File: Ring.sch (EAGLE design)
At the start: 23 parts, among them U1 BQ25125YFPR, U3 NRF52832-CIAA-R

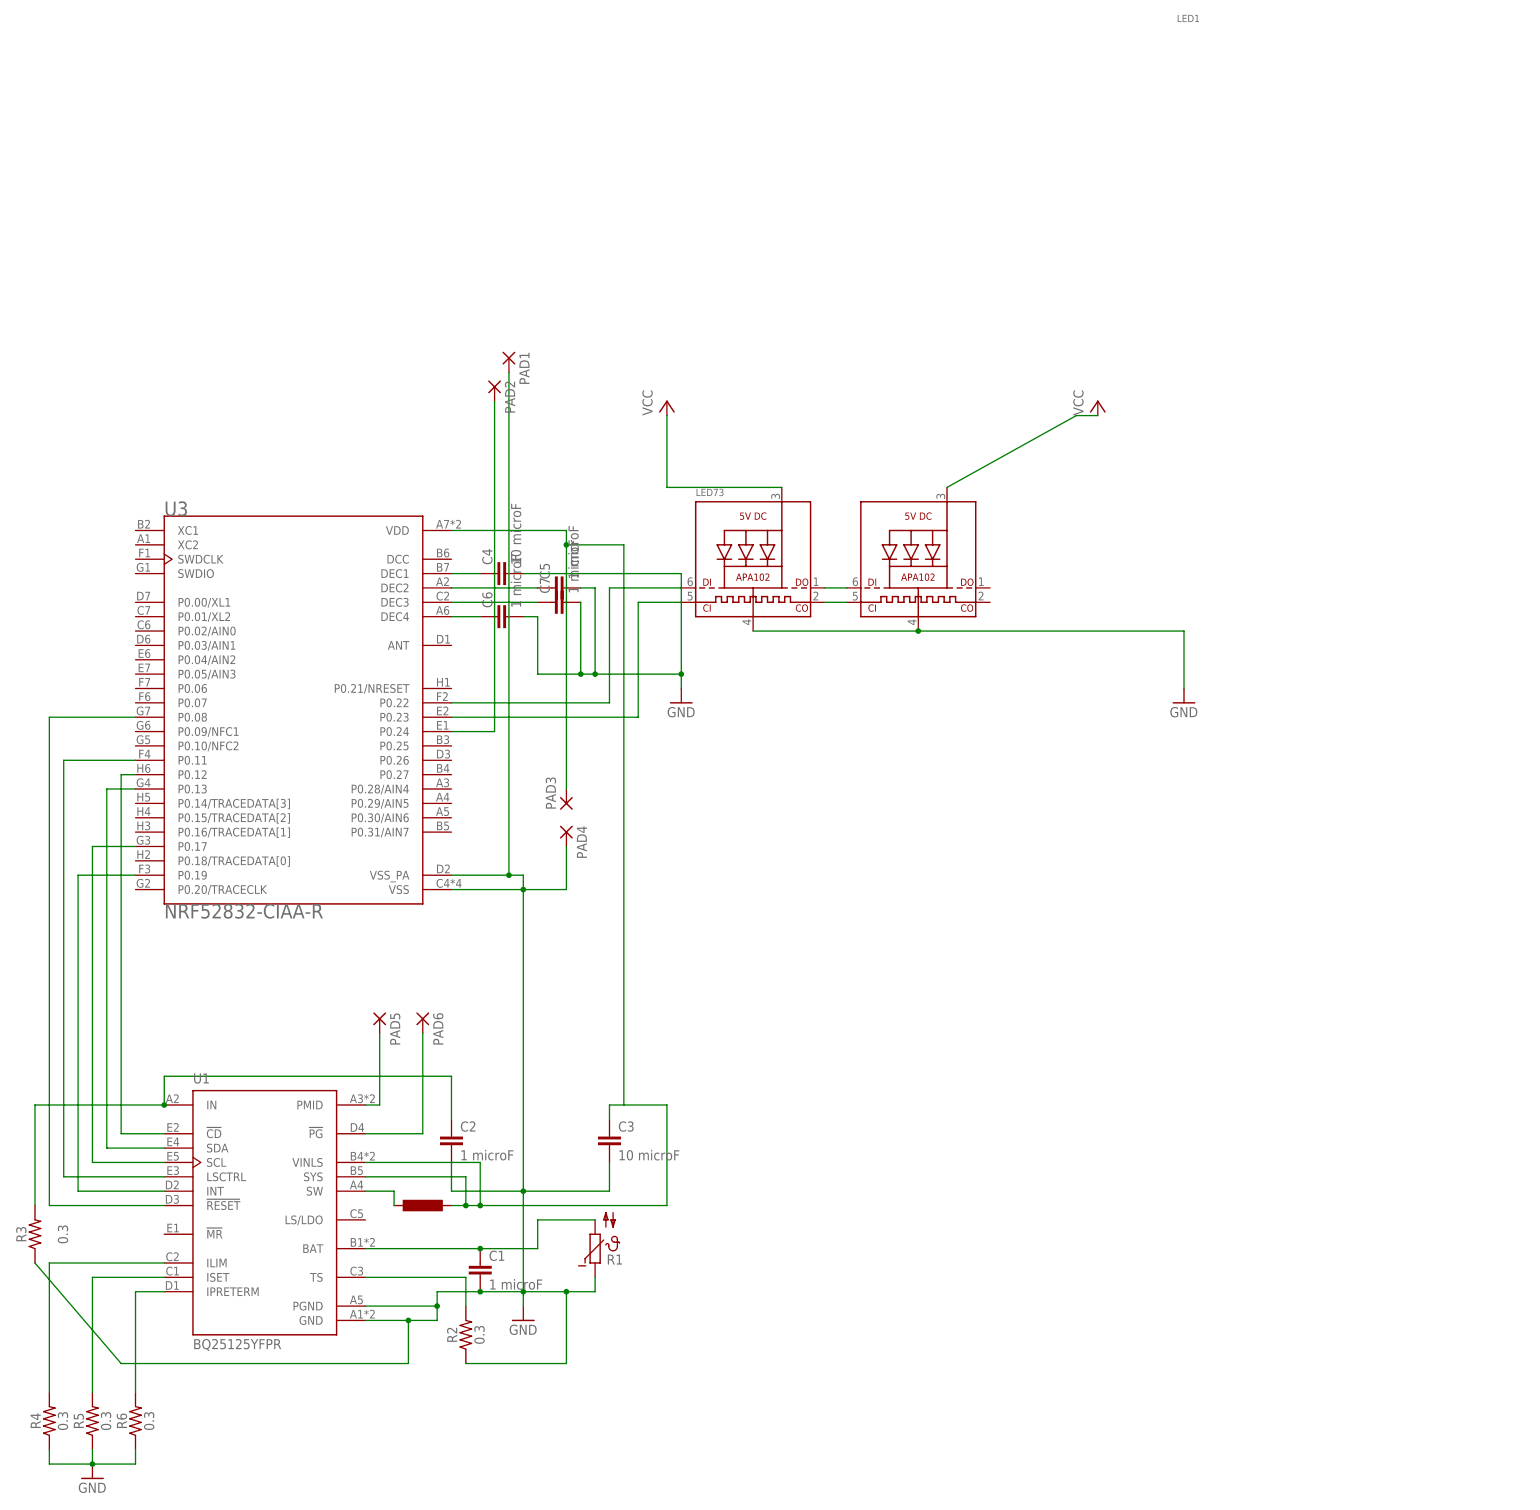
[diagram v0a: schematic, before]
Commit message: Created New schemtatic
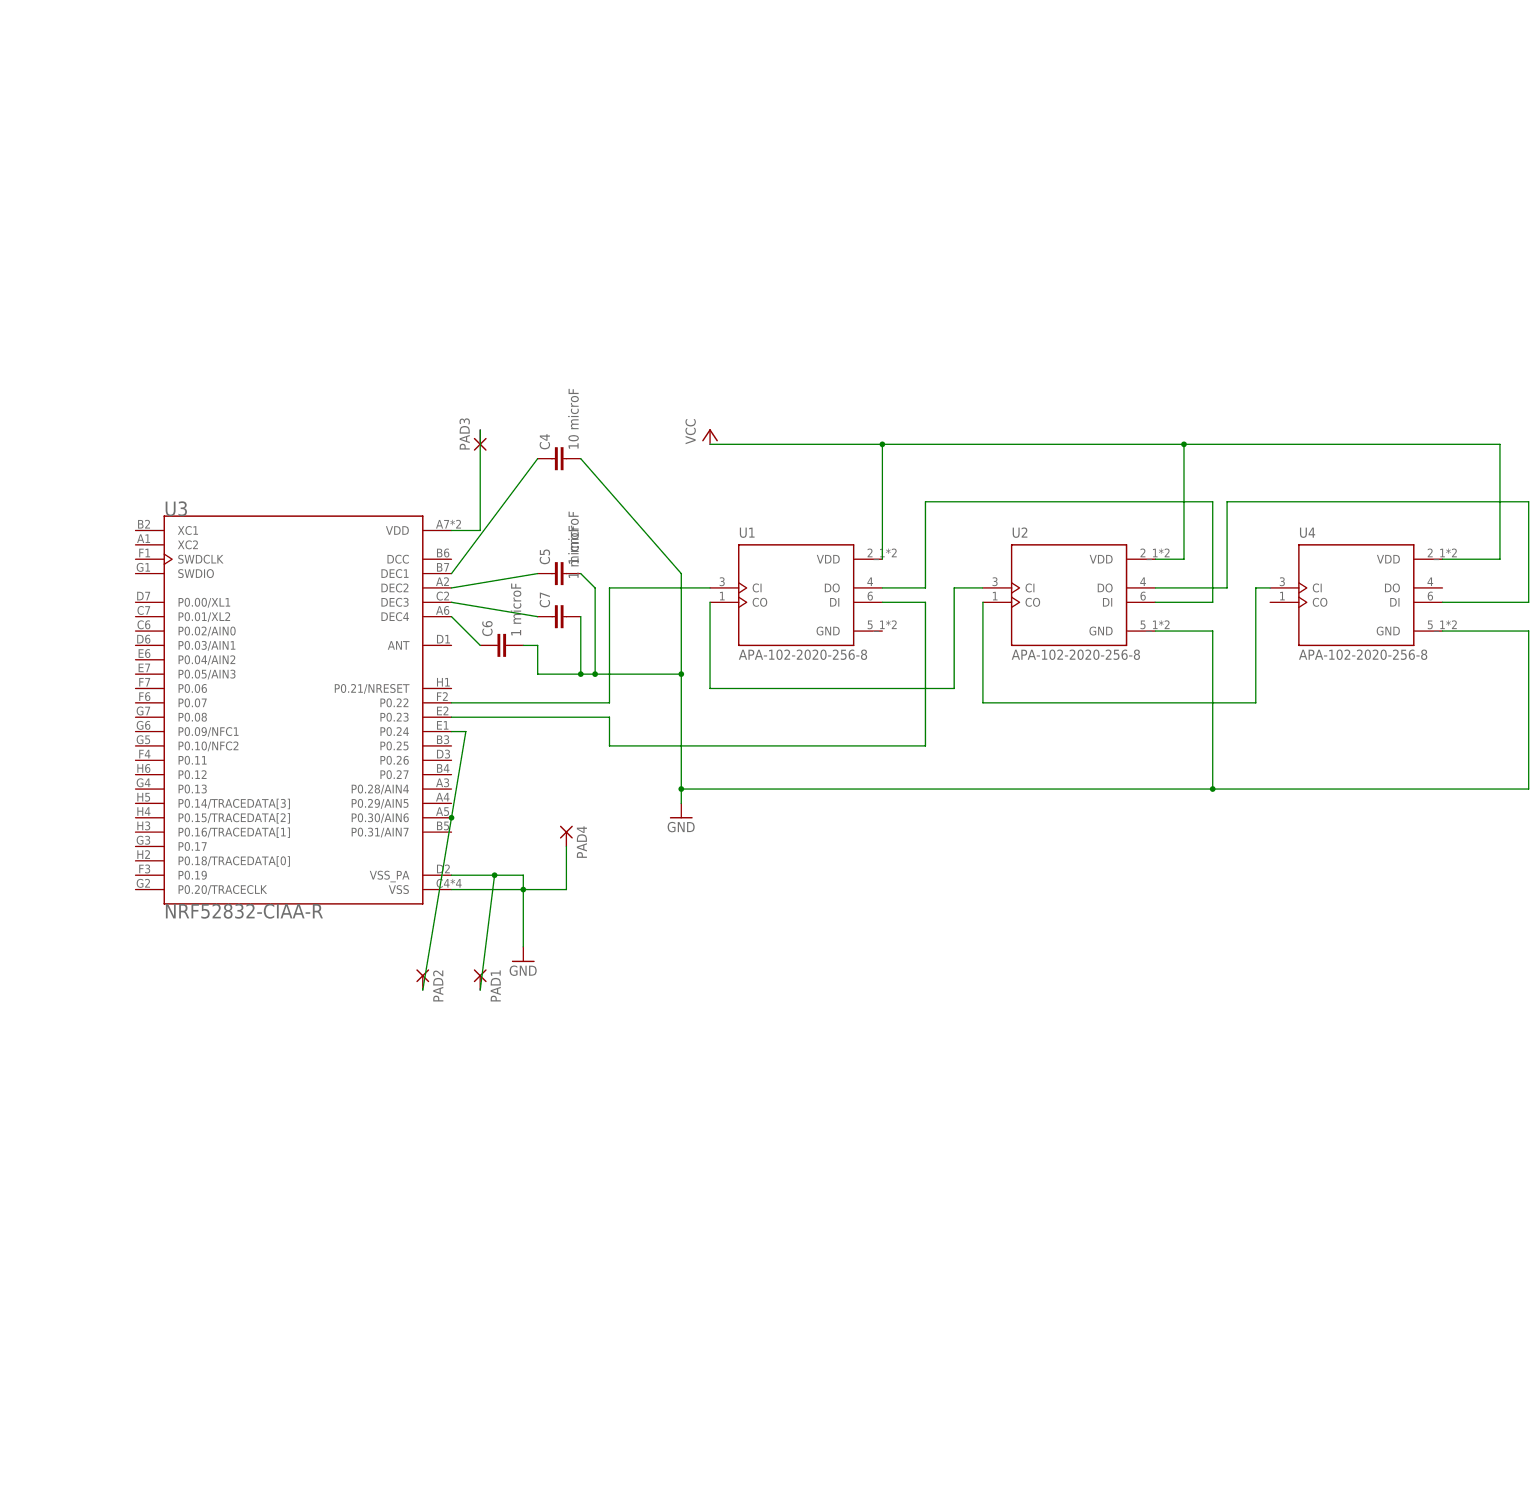
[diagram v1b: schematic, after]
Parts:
- removed C1, C2: 1 microF, capacitor-wima:C2,5-3
- removed C3: 10 microF, capacitor-wima:C2,5-3
- removed LED1, LED73: (no value), microbuilder:APA1022020
- removed PAD5, PAD6: (no value), wirepad:1,6/0,8
- removed R1: (no value), ptc-ntc:NTC640
- removed R2, R3, R4, R5, R6: 0.3, SparkFun-Resistors:0.3OHM-0805-1/8W-1%
- added U2, U4: APA-102-2020-256-8, APA-102-2020-256-8:APA-102-2020-256-8
- U1: value BQ25125YFPR -> APA-102-2020-256-8; device BQ25125YFPR:BQ25125YFPR -> APA-102-2020-256-8:APA-102-2020-256-8
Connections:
- removed net N$1: LED1.DI, LED73.DO
- removed net N$10: U1.SCL, U3.P0.17
- removed net N$11: U1.INT, U3.P0.19
- removed net N$12: U1.!RESET, U3.P0.08
- removed net N$13: C2.1, R3.2, U1.IN
- removed net N$14: R2.2, U1.TS
- removed net N$16: U1.SW
- removed net N$17: R5.2, U1.ISET
- removed net N$19: R6.2, U1.IPRETERM
- removed net N$24: PAD5.P, U1.PMID
- removed net N$25: PAD6.P, U1.!PG
- removed net N$3: LED1.CKI, LED73.CKO
- removed net N$9: U1.SDA, U3.P0.13
- net GND: now also U2.GND, U4.GND; no longer C1.2, C2.2, C3.2, LED1.GND, LED73.GND, R1.1, R2.1, R3.1, R4.1, R5.1, R6.1, U1.GND, U1.PGND
- net N$15: now also U3.P0.30/AIN6
- net N$18: no longer C3.1, U1.SYS, U1.VINLS
- net N$2: now also U1.CO, U2.CI; no longer R4.2, U1.ILIM
- net N$4: now also U1.CI; no longer LED73.DI
- net N$5: now also U1.DI; no longer LED73.CKI
- net N$6: now also U1.DO, U2.DI; no longer C1.1, R1.2, U1.BAT
- net N$7: now also U2.CO, U4.CI; no longer U1.!CD, U3.P0.12
- net N$8: now also U2.DO, U4.DI; no longer U1.LSCTRL, U3.P0.11
- net VCC: now also U1.VDD, U2.VDD, U4.VDD; no longer LED1.VDD, LED73.VDD
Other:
- moved on the sheet: C4, C5, C6, C7, PAD1, PAD2, PAD3

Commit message: projects added
added projects
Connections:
- net N$15: no longer U3.P0.30/AIN6
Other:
- moved on the sheet: PAD1, PAD2
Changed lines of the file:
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@@
 <attribute name="VALUE" x="91.44" y="139.7" size="1.778" layer="96"/>
 </instance>
-<instance part="PAD1" gate="P" x="86.36" y="139.7" smashed="yes" rot="R270">
-<attribute name="NAME" x="88.2142" y="140.843" size="1.778" layer="95" rot="R270"/>
-<attribute name="VALUE" x="83.058" y="140.843" size="1.778" layer="96" rot="R270"/>
+<instance part="PAD1" gate="P" x="88.9" y="162.56" smashed="yes" rot="R270">
+<attribute name="NAME" x="90.7542" y="163.703" size="1.778" layer="95" rot="R270"/>
+<attribute name="VALUE" x="85.598" y="163.703" size="1.778" layer="96" rot="R270"/>
 </instance>
-<instance part="PAD2" gate="P" x="76.2" y="139.7" smashed="yes" rot="R270">
-<attribute name="NAME" x="78.0542" y="140.843" size="1.778" layer="95" rot="R270"/>
-<attribute name="VALUE" x="72.898" y="140.843" size="1.778" layer="96" rot="R270"/>
+<instance part="PAD2" gate="P" x="99.06" y="175.26" smashed="yes" rot="R90">
+<attribute name="NAME" x="97.2058" y="174.117" size="1.778" layer="95" rot="R90"/>
+<attribute name="VALUE" x="102.362" y="174.117" size="1.778" layer="96" rot="R90"/>
 </instance>
 <instance part="C4" gate="G$1" x="99.06" y="231.14" smashed="yes" rot="R90">
@@
 <pinref part="GND1" gate="1" pin="GND"/>
 <wire x1="93.98" y1="144.78" x2="93.98" y2="154.94" width="0.1524" layer="91"/>
-<wire x1="88.9" y1="157.48" x2="86.36" y2="137.16" width="0.1524" layer="91"/>
+<wire x1="88.9" y1="157.48" x2="88.9" y2="160.02" width="0.1524" layer="91"/>
 <junction x="88.9" y="157.48"/>
 <pinref part="PAD1" gate="P" pin="P"/>
@@
 <segment>
 <pinref part="U3" gate="G$1" pin="P0.24"/>
-<wire x1="81.28" y1="182.88" x2="83.82" y2="182.88" width="0.1524" layer="91"/>
-<wire x1="83.82" y1="182.88" x2="81.28" y2="167.64" width="0.1524" layer="91"/>
 <pinref part="PAD2" gate="P" pin="P"/>
-<pinref part="U3" gate="G$1" pin="P0.30/AIN6"/>
-<wire x1="81.28" y1="167.64" x2="76.2" y2="137.16" width="0.1524" layer="91"/>
-<junction x="81.28" y="167.64"/>
+<wire x1="81.28" y1="182.88" x2="99.06" y2="182.88" width="0.1524" layer="91"/>
+<wire x1="99.06" y1="182.88" x2="99.06" y2="177.8" width="0.1524" layer="91"/>
 </segment>
 </net>
